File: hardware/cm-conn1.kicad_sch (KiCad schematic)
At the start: 7 parts, among them J5 RJ45_RB1-125B8G1A

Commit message: feat: add InvenTree IPN field to all schematic symbols
102 components mapped to 41 unique InvenTree part numbers.
IPN format: category prefix + sequential number (e.g. C-001, R-002, U-009).
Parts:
- C22: IPN (none) -> C-001
- CM1: IPN (none) -> J-002
- J5: IPN (none) -> J-008
- R10, R12: IPN (none) -> R-018
- R13: IPN (none) -> R-001
- R16: IPN (none) -> R-002
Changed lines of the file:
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@@
+			)
+		)
+		(property "IPN" "C-001"
+			(at 0 0 0)
+			(show_name no)
+			(do_not_autoplace no)
+			(hide yes)
+			(effects
+				(font
+					(size 1.27 1.27)
+				)
 			)
 		)
@@
 			)
 		)
+		(property "IPN" "J-002"
+			(at 0 0 0)
+			(show_name no)
+			(do_not_autoplace no)
+			(hide yes)
+			(effects
+				(font
+					(size 1.27 1.27)
+				)
+			)
+		)
 		(pin "1"
 		)
@@
 			)
 		)
+		(property "IPN" "J-008"
+			(at 0 0 0)
+			(show_name no)
+			(do_not_autoplace no)
+			(hide yes)
+			(effects
+				(font
+					(size 1.27 1.27)
+				)
+			)
+		)
 		(pin "R2"
 		)
@@
 			)
 		)
+		(property "IPN" "R-001"
+			(at 0 0 0)
+			(show_name no)
+			(do_not_autoplace no)
+			(hide yes)
+			(effects
+				(font
+					(size 1.27 1.27)
+				)
+			)
+		)
 		(pin "1"
 		)
@@
 			)
 		)
+		(property "IPN" "R-002"
+			(at 0 0 0)
+			(show_name no)
+			(do_not_autoplace no)
+			(hide yes)
+			(effects
+				(font
+					(size 1.27 1.27)
+				)
+			)
+		)
 		(pin "1"
 		)
@@
 			(show_name no)
 			(do_not_autoplace no)
+			(effects
+				(font
+					(size 1.27 1.27)
+				)
+			)
+		)
+		(property "IPN" "R-018"
+			(at 0 0 0)
+			(show_name no)
+			(do_not_autoplace no)
+			(hide yes)
 			(effects
 				(font
@@
 			(effects
 				(font
+					(size 1.27 1.27)
+				)
+			)
+		)
+		(property "IPN" "R-018"
+			(at 0 0 0)
+			(show_name no)
+			(do_not_autoplace no)
+			(hide yes)
+			(effects
+				(font

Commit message: chore: remove redundant supplier fields, keep IPN as single link to InvenTree
Removed: Supplier, Digikey, Notes, KiLib_Generator, Mouser, Arrow fields.
InvenTree IPN is now the only external reference in the schematic.
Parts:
- C22: Digikey 1276-1180-1-ND -> (none); KiLib_Generator SMD_2terminal_chip_molded -> (none); Notes 10% 16V Ceramic Capacitor X7R -> (none); Supplier https://www.digikey.ch/de/products/detail/samsung-electro-m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 -> (none)
- CM1: Notes DF40C-100DS-0.4V(51) -> (none); Supplier https://www.digikey.ch/de/products/detail/hirose-electric-c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 -> (none)
- R10, R12, R13, R16: KiLib_Generator SMD_2terminal_chip_molded -> (none)
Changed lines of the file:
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@@
-			)
-		)
-		(property "Supplier" "https://www.digikey.ch/de/products/detail/samsung-electro-mechanics/CL21B104KBCNNNC/3886661"
-			(at 187.96 73.66 0)
-			(hide yes)
-			(show_name no)
-			(do_not_autoplace no)
-			(effects
-				(font
-					(size 1.27 1.27)
-				)
-			)
-		)
-		(property "Notes" "10% 16V Ceramic Capacitor X7R"
-			(at 187.96 73.66 0)
-			(hide yes)
-			(show_name no)
-			(do_not_autoplace no)
-			(effects
-				(font
-					(size 1.27 1.27)
-				)
-			)
-		)
-		(property "Digikey" "1276-1180-1-ND"
-			(at 187.96 73.66 0)
-			(hide yes)
-			(show_name no)
-			(do_not_autoplace no)
-			(effects
-				(font
-					(size 1.27 1.27)
-				)
-			)
-		)
-		(property "KiLib_Generator" "SMD_2terminal_chip_molded"
-			(at 187.96 73.66 0)
-			(hide yes)
-			(show_name no)
-			(do_not_autoplace no)
-			(effects
-				(font
-					(size 1.27 1.27)
-				)
 			)
 		)
 		(property "IPN" "C-001"
 			(at 0 0 0)
-			(show_name no)
-			(do_not_autoplace no)
-			(hide yes)
+			(hide yes)
+			(show_name no)
+			(do_not_autoplace no)
 			(effects
 				(font
@@
 			)
 		)
-		(property "Notes" "DF40C-100DS-0.4V(51)"
-			(at 87.63 96.52 0)
-			(hide yes)
-			(show_name no)
-			(do_not_autoplace no)
-			(effects
-				(font
-					(size 1.27 1.27)
-				)
-			)
-		)
-		(property "Supplier" "https://www.digikey.ch/de/products/detail/hirose-electric-co-ltd/DF40C-100DS-0-4V-51/1969476"
-			(at 87.63 96.52 0)
-			(hide yes)
-			(show_name no)
-			(do_not_autoplace no)
-			(effects
-				(font
-					(size 1.27 1.27)
-				)
-			)
-		)
 		(property "IPN" "J-002"
 			(at 0 0 0)
-			(show_name no)
-			(do_not_autoplace no)
-			(hide yes)
+			(hide yes)
+			(show_name no)
+			(do_not_autoplace no)
 			(effects
 				(font
@@
 		(property "IPN" "J-008"
 			(at 0 0 0)
-			(show_name no)
-			(do_not_autoplace no)
-			(hide yes)
+			(hide yes)
+			(show_name no)
+			(do_not_autoplace no)
 			(effects
 				(font
@@
 			)
 		)
-		(property "KiLib_Generator" "SMD_2terminal_chip_molded"
-			(at 182.88 69.85 0)
-			(hide yes)
-			(show_name no)
-			(do_not_autoplace no)
-			(effects
-				(font
-					(size 1.27 1.27)
-				)
-			)
-		)
 		(property "IPN" "R-001"
 			(at 0 0 0)
-			(show_name no)
-			(do_not_autoplace no)
-			(hide yes)
+			(hide yes)
+			(show_name no)
+			(do_not_autoplace no)
 			(effects
 				(font
@@
 			)
 		)
-		(property "KiLib_Generator" "SMD_2terminal_chip_molded"
-			(at 153.67 160.02 0)
-			(hide yes)
-			(show_name no)
-			(do_not_autoplace no)
-			(effects
-				(font
-					(size 1.27 1.27)
-				)
-			)
-		)
 		(property "IPN" "R-002"
 			(at 0 0 0)
-			(show_name no)
-			(do_not_autoplace no)
-			(hide yes)
+			(hide yes)
+			(show_name no)
+			(do_not_autoplace no)
 			(effects
 				(font
@@
 			)
 		)
-		(property "KiLib_Generator" "SMD_2terminal_chip_molded"
-			(at 234.95 58.42 0)
-			(hide yes)
-			(show_name no)
-			(do_not_autoplace no)
-			(effects
-				(font
-					(size 1.27 1.27)
-				)
-			)
-		)
 		(property "IPN" "R-018"
 			(at 0 0 0)
-			(show_name no)
-			(do_not_autoplace no)
-			(hide yes)
+			(hide yes)
+			(show_name no)
+			(do_not_autoplace no)
 			(effects
 				(font
@@
 			)
 		)
-		(property "KiLib_Generator" "SMD_2terminal_chip_molded"
-			(at 229.87 58.42 0)
-			(hide yes)
-			(show_name no)
-			(do_not_autoplace no)
-			(effects
-				(font
-					(size 1.27 1.27)
-				)
-			)
-		)
 		(property "IPN" "R-018"
 			(at 0 0 0)
-			(show_name no)
-			(do_not_autoplace no)
-			(hide yes)
-			(effects
-				(font
+			(hide yes)
+			(show_name no)
+			(do_not_autoplace no)
+			(effects
+				(font

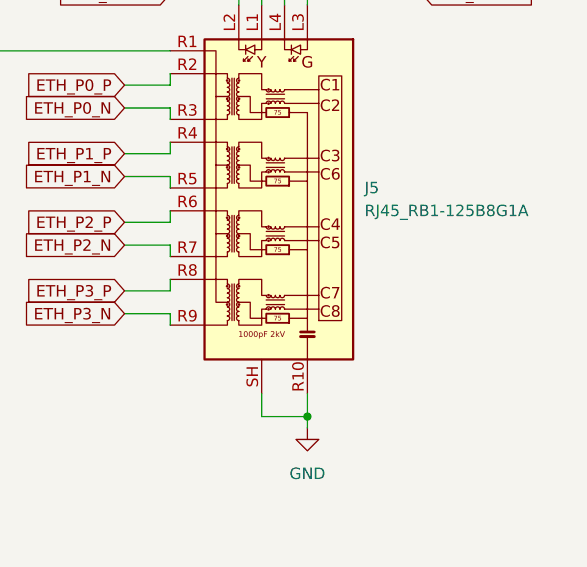
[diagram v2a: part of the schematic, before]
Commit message: wip: HR911130A RJ45 MagJack symbol and footprint (not routed)
Hanrun HR911130A GbE MagJack as replacement for RB1-125B8G1A.
Signal pins are on opposite side — requires full re-route of Ethernet area.
Parked for later.
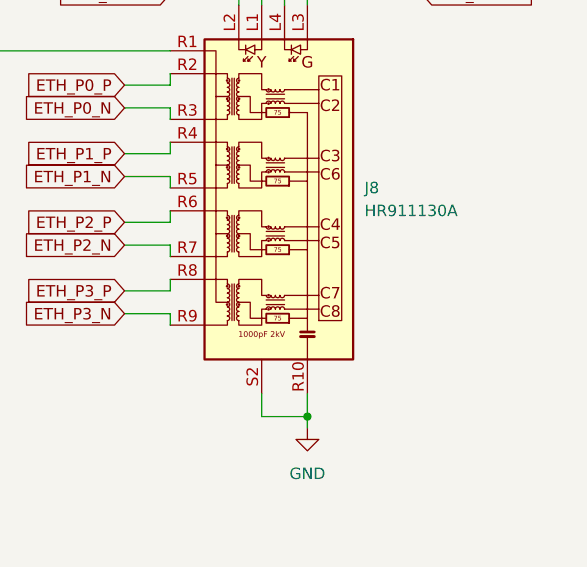
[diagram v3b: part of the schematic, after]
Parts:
- removed J5: RJ45_RB1-125B8G1A, Connector_RJ:RJ45_UDE_RB1-125B8G1A, symbol Connector:RJ45_RB1-125B8G1A
- added J8: HR911130A, granit:HANRUN_HR911130A, symbol granit:HR911130A
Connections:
- net ETH_P0_N: now also J8.R3 (TD1-)
- net ETH_P0_P: now also J8.R2 (TD1+)
- net ETH_P1_N: now also J8.R5 (TD2-)
- net ETH_P1_P: now also J8.R4 (TD2+)
- net ETH_P2_N: now also J8.R7 (TD3-)
- net ETH_P2_P: now also J8.R6 (TD3+)
- net ETH_P3_N: now also J8.R9 (TD4-)
- net ETH_P3_P: now also J8.R8 (TD4+)
- net ETH_nLED1: now also J8.L4
- net ETH_nLED2: now also J8.L2
- net GND: now also J8.R10 (GND), J8.S2 (SH)
- net at C22.1, R13.2: now also J8.R1 (CT_PRI)
- net at R10.2: now also J8.L1
- net at R12.2: now also J8.L3
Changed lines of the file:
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@@
+	)
+	(symbol
+		(lib_id "granit:HR911130A")
+		(at 232.41 87.63 0)
+		(mirror y)
+		(unit 1)
+		(body_style 1)
+		(exclude_from_sim no)
+		(in_bom yes)
+		(on_board yes)
+		(in_pos_files yes)
+		(dnp no)
+		(fields_autoplaced yes)
+		(property "Reference" "J8"
+			(at 241.3 85.0899 0)
+			(show_name no)
+			(do_not_autoplace no)
+			(effects
+				(font
+					(size 1.27 1.27)
+				)
+				(justify right)
+			)
+		)
+		(property "Value" "HR911130A"
+			(at 241.3 87.6299 0)
+			(show_name no)
+			(do_not_autoplace no)
+			(effects
+				(font
+					(size 1.27 1.27)
+				)
+				(justify right)
+			)
+		)
+		(property "Footprint" "granit:HANRUN_HR911130A"
+			(at 231.14 85.09 0)
+			(hide yes)
+			(show_name no)
+			(do_not_autoplace no)
+			(effects
+				(font
+					(size 1.27 1.27)
+				)
+			)
+		)
+		(property "Datasheet" "https://datasheet.lcsc.com/szlcsc/1901091107_UDE-Corp-RB1-125B8G1A_C363353.pdf"
+			(at 238.506 86.487 0)
+			(hide yes)
+			(show_name no)
+			(do_not_autoplace no)
+			(effects
+				(font
+					(size 1.27 1.27)
+				)
+				(justify left top)
+			)
+		)
+		(property "Description" "GbE MagJack with integrated magnetics, Hanrun HR911130A"
+			(at 232.41 87.63 0)
+			(hide yes)
+			(show_name no)
+			(do_not_autoplace no)
+			(effects
+				(font
+					(size 1.27 1.27)
+				)
+			)
+		)
+		(pin "R3"
+		)
+		(pin "L1"
+		)
+		(pin "L4"
+		)
+		(pin "R5"
+		)
+		(pin "L2"
+		)
+		(pin "R9"
+		)
+		(pin "R8"
+		)
+		(pin "R2"
+		)
+		(pin "L3"
+		)
+		(pin "R7"
+		)
+		(pin "R4"
+		)
+		(pin "R1"
+		)
+		(pin "R6"
+		)
+		(pin "S2"
+		)
+		(pin "R10"
+		)
+		(instances
+			(project "granit"
+				(path "/d2c135e3-a983-4cd4-8cff-b50ca3c7671a/425bdf56-ee3a-43f6-b6d9-8fa9cc85dc16"
+					(reference "J8")
+					(unit 1)
+				)
+			)
+		)
 	)
 	(symbol
@@
 					(unit 1)
 				)
-			)
-		)
-	)
-	(symbol
-		(lib_id "Connector:RJ45_RB1-125B8G1A")
-		(at 232.41 87.63 0)
-		(mirror y)
-		(unit 1)
-		(body_style 1)
-		(exclude_from_sim no)
-		(in_bom yes)
-		(on_board yes)
-		(in_pos_files yes)
-		(dnp no)
-		(property "Reference" "J5"
-			(at 241.3 85.0899 0)
-			(show_name no)
-			(do_not_autoplace no)
-			(effects
-				(font
-					(size 1.27 1.27)
-				)
-				(justify right)
-			)
-		)
-		(property "Value" "RJ45_RB1-125B8G1A"
-			(at 241.3 87.6299 0)
-			(show_name no)
-			(do_not_autoplace no)
-			(effects
-				(font
-					(size 1.27 1.27)
-				)
-				(justify right)
-			)
-		)
-		(property "Footprint" "Connector_RJ:RJ45_UDE_RB1-125B8G1A"
-			(at 231.14 85.09 0)
-			(hide yes)
-			(show_name no)
-			(do_not_autoplace no)
-			(effects
-				(font
-					(size 1.27 1.27)
-				)
-			)
-		)
-		(property "Datasheet" "https://datasheet.lcsc.com/szlcsc/1901091107_UDE-Corp-RB1-125B8G1A_C363353.pdf"
-			(at 238.506 86.487 0)
-			(hide yes)
-			(show_name no)
-			(do_not_autoplace no)
-			(effects
-				(font
-					(size 1.27 1.27)
-				)
-				(justify left top)
-			)
-		)
-		(property "Description" "LAN Transformer Jack, RJ45, 10/100/1000 BaseT"
-			(at 232.41 87.63 0)
-			(hide yes)
-			(show_name no)
-			(do_not_autoplace no)
-			(effects
-				(font
-					(size 1.27 1.27)
-				)
-			)
-		)
-		(property "IPN" "J-008"
-			(at 0 0 0)
-			(hide yes)
-			(show_name no)
-			(do_not_autoplace no)
-			(effects
-				(font
-					(size 1.27 1.27)
-				)
-			)
-		)
-		(pin "R2"
-		)
-		(pin "SH"
-		)
-		(pin "L2"
-		)
-		(pin "R4"
-		)
-		(pin "R1"
-		)
-		(pin "R6"
-		)
-		(pin "R5"
-		)
-		(pin "R8"
-		)
-		(pin "L4"
-		)
-		(pin "L1"
-		)
-		(pin "R3"
-		)
-		(pin "R9"
-		)
-		(pin "L3"
-		)
-		(pin "R7"
-		)
-		(pin "R10"
-		)
-		(instances
-			(project "granit"
-				(path "/d2c135e3-a983-4cd4-8cff-b50ca3c7671a/425bdf56-ee3a-43f6-b6d9-8fa9cc85dc16"
-					(reference "J5")
-					(unit 1)
-				)

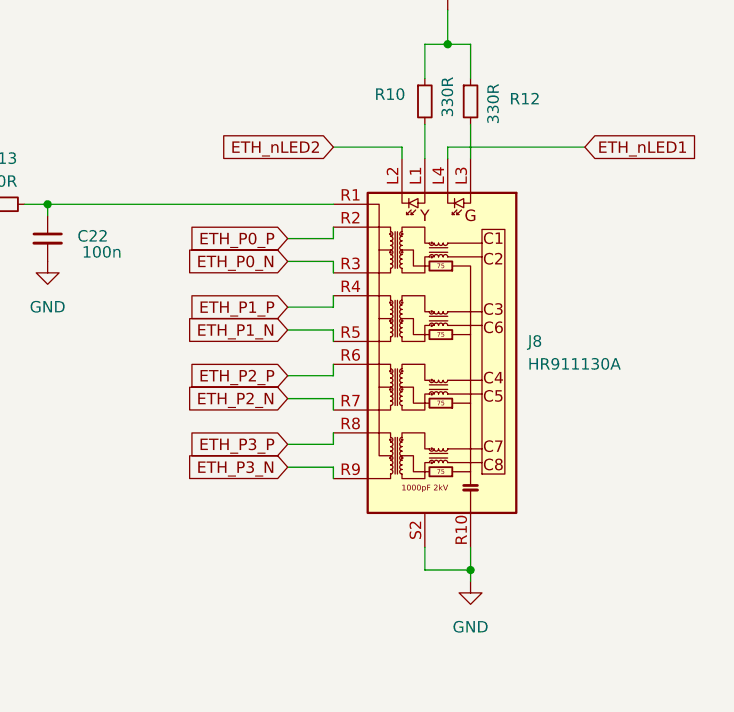
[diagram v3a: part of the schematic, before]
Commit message: feat: swap RJ45 MagJack to HR911130A (Hanrun GbE)
- New symbol and footprint in granit library
- Pin mapping follows TIA-568B MDI standard
- All 4 Ethernet diff pairs routed with 100Ω impedance
- Pair 1 uses via + bottom trace for length matching
- DRC: 0 violations, 0 unconnected, 0 parity issues
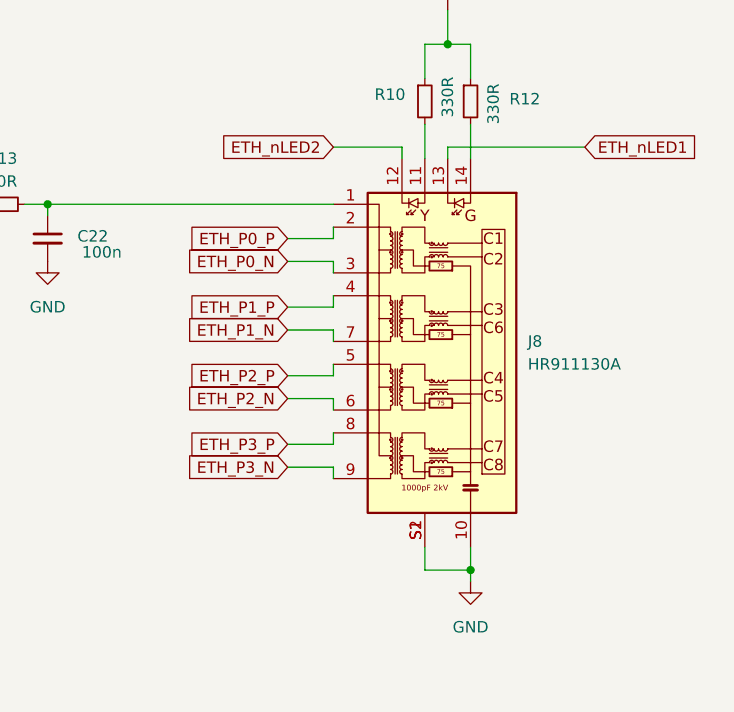
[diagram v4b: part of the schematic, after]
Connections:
- net ETH_P0_N: now also J8.3 (TD1-); no longer J8.R3 (TD1-)
- net ETH_P0_P: now also J8.2 (TD1+); no longer J8.R2 (TD1+)
- net ETH_P1_N: now also J8.7 (TD2-); no longer J8.R5 (TD2-)
- net ETH_P1_P: now also J8.4 (TD2+); no longer J8.R4 (TD2+)
- net ETH_P2_N: now also J8.6 (TD3-); no longer J8.R7 (TD3-)
- net ETH_P2_P: now also J8.5 (TD3+); no longer J8.R6 (TD3+)
- net ETH_P3_N: now also J8.9 (TD4-); no longer J8.R9 (TD4-)
- net ETH_P3_P: now also J8.8 (TD4+); no longer J8.R8 (TD4+)
- net ETH_nLED1: now also J8.13; no longer J8.L4
- net ETH_nLED2: now also J8.12; no longer J8.L2
- net GND: now also J8.10 (GND), J8.S1 (SH); no longer J8.R10 (GND)
- net at C22.1, R13.2: now also J8.1 (CT_PRI); no longer J8.R1 (CT_PRI)
- net at R10.2: now also J8.11; no longer J8.L1
- net at R12.2: now also J8.14; no longer J8.L3
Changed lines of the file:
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@@
 			)
 		)
-		(pin "R3"
+		(pin "3"
 		)
-		(pin "L1"
+		(pin "8"
 		)
-		(pin "L4"
+		(pin "1"
 		)
-		(pin "R5"
+		(pin "4"
 		)
-		(pin "L2"
+		(pin "11"
 		)
-		(pin "R9"
+		(pin "13"
 		)
-		(pin "R8"
+		(pin "5"
 		)
-		(pin "R2"
+		(pin "14"
 		)
-		(pin "L3"
+		(pin "S1"
 		)
-		(pin "R7"
+		(pin "6"
 		)
-		(pin "R4"
+		(pin "12"
 		)
-		(pin "R1"
+		(pin "9"
 		)
-		(pin "R6"
+		(pin "7"
 		)
 		(pin "S2"
 		)
-		(pin "R10"
+		(pin "2"
+		)
+		(pin "10"
 		)
 		(instances

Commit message: fix: add missing IPNs for J4 (SATA), J5 (HR911130A), Y1 (crystal)
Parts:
- J8: IPN (none) -> J-008
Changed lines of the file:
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@@
+			)
+		)
+		(property "IPN" "J-008"
+			(at 232.41 87.63 0)
+			(hide yes)
+			(show_name no)
+			(do_not_autoplace no)
+			(effects
+				(font
+					(size 1.27 1.27)
+				)
 			)
 		)
